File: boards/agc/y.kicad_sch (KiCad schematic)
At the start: 2 parts, among them T1 2:1

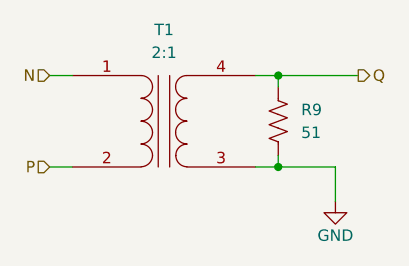
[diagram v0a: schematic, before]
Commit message: Add PSA switching modules and rework fine ref
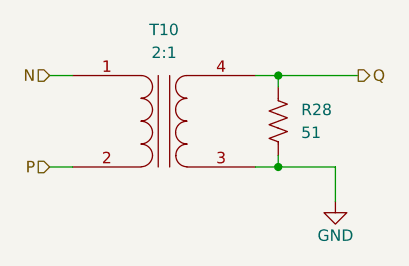
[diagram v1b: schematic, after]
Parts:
- renumbered R9 to R28, T1 to T10
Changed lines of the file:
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@@
 (kicad_sch
-	(version 20231120)
+	(version 20250114)
 	(generator "eeschema")
-	(generator_version "8.0")
+	(generator_version "9.0")
 	(paper "A4")
 	(junction
@@
 		(shape input)
 		(at 52.07 62.23 180)
-		(fields_autoplaced yes)
 		(effects
 			(font
@@
 		(shape output)
 		(at 86.36 52.07 0)
-		(fields_autoplaced yes)
 		(effects
 			(font
@@
 		(shape input)
 		(at 52.07 52.07 180)
-		(fields_autoplaced yes)
 		(effects
 			(font
@@
 		(dnp no)
 		(fields_autoplaced yes)
-		(property "Reference" "R9"
+		(property "Reference" "R28"
 			(at 80.01 55.8799 0)
 			(effects
@@
 		(on_board yes)
 		(dnp no)
-		(property "Reference" "#PWR031"
+		(property "Reference" "#PWR030"
 			(at 83.82 72.39 0)
 			(effects
@@
 		(dnp no)
 		(fields_autoplaced yes)
-		(property "Reference" "T1"
+		(property "Reference" "T10"
 			(at 64.7827 46.99 0)
 			(effects
